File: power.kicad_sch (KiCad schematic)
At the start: 53 parts, among them J10 Conn_01x02, J11 Solar_Cell, J2 USB_C_Receptacle_USB2.0_14P, J9 Battery_Cell, Q1 AO4882, Q3 AO4882, U2 BQ25798, U5 TPS6282x

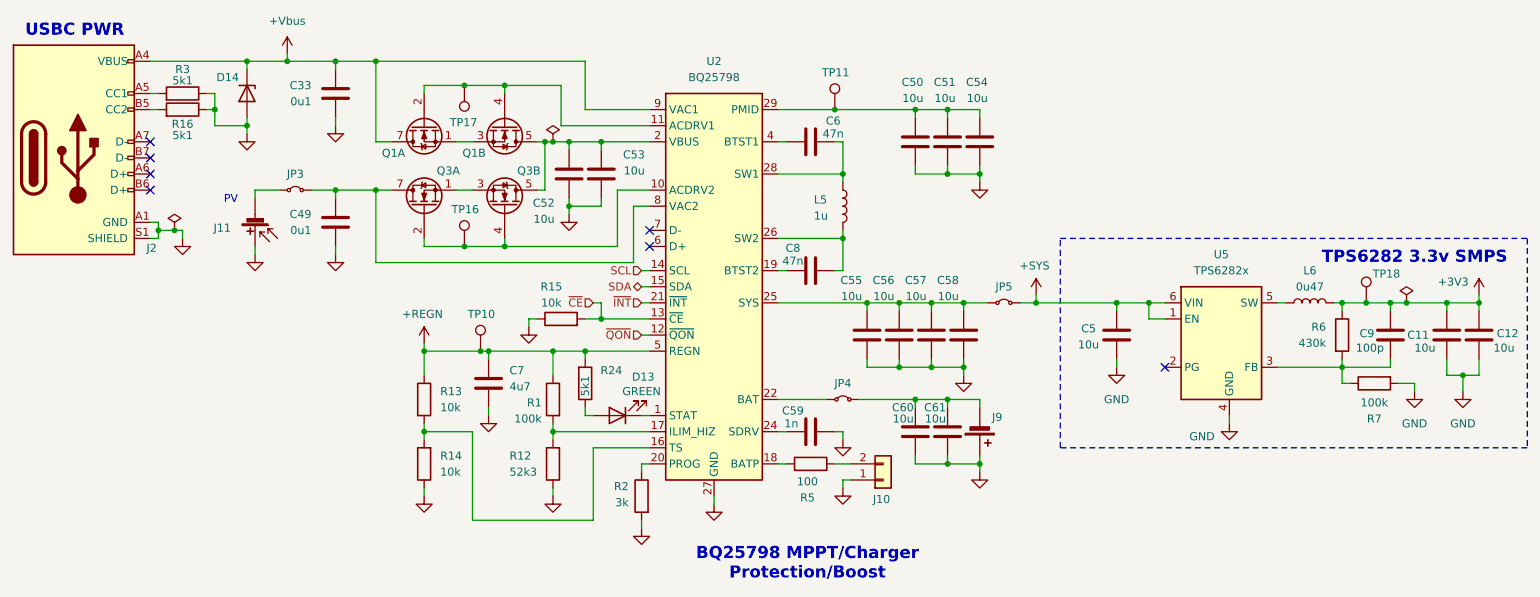
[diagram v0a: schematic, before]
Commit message: schem: renumber
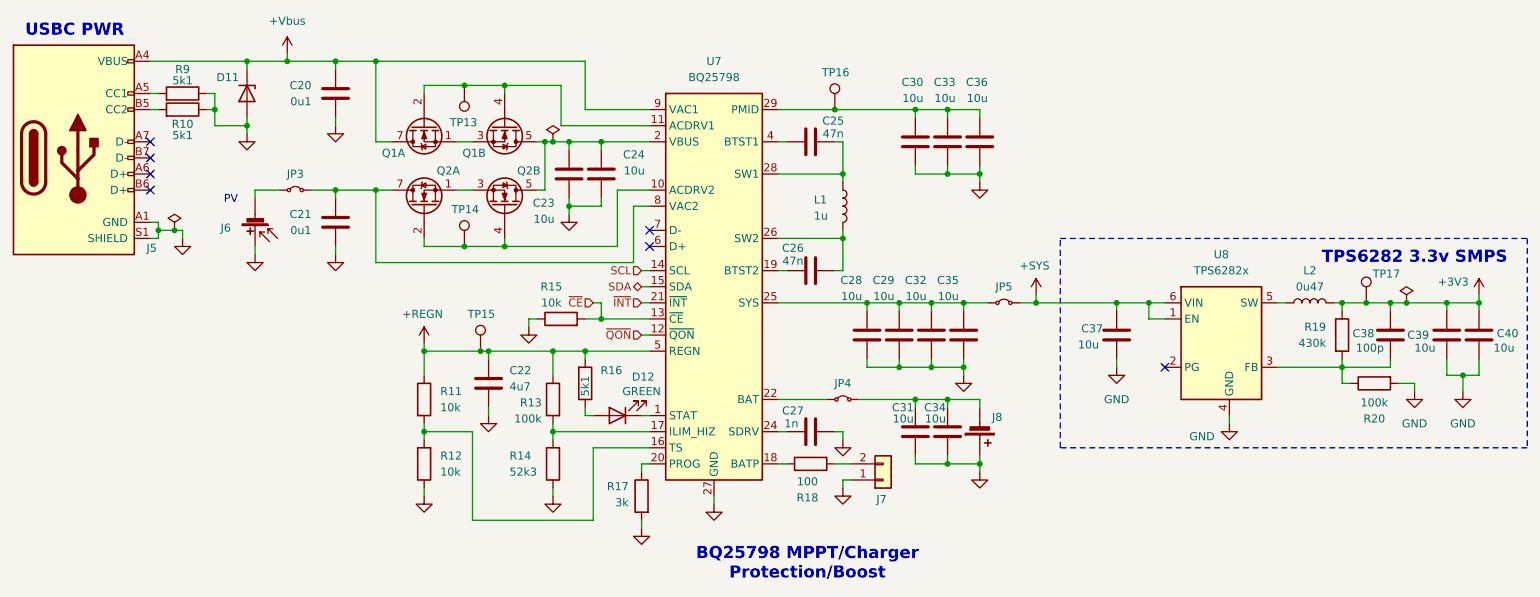
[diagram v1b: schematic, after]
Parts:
- renumbered C33 to C20, C49 to C21, C7 to C22, C52 to C23, C53 to C24, C6 to C25, C8 to C26, C59 to C27, C55 to C28, C56 to C29, C50 to C30, C60 to C31, C57 to C32, C51 to C33, C61 to C34, C58 to C35, C54 to C36, C5 to C37, C9 to C38, C11 to C39, C12 to C40, D14 to D11, D13 to D12, J2 to J5, J11 to J6, J10 to J7, J9 to J8, L5 to L1, L6 to L2, Q3 to Q2, R16 to R10, R13 to R11, R14 to R12, R1 to R13, R12 to R14, R24 to R16, R2 to R17, R5 to R18, R6 to R19, R7 to R20, R3 to R9, TP17 to TP13, TP16 to TP14, TP10 to TP15, TP11 to TP16, TP18 to TP17, U2 to U7, U5 to U8

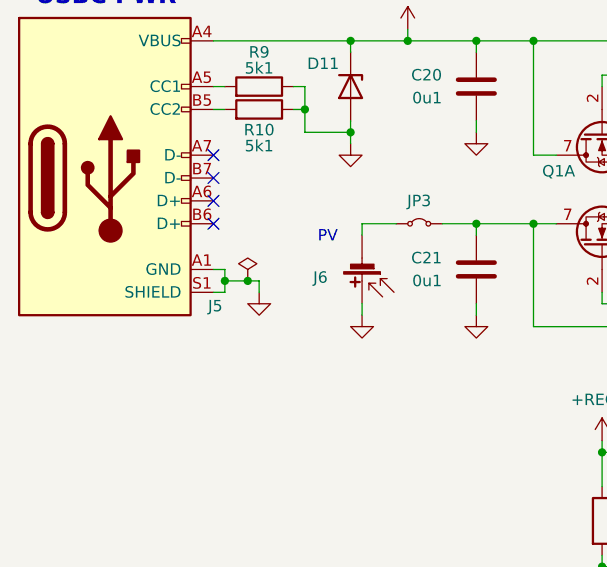
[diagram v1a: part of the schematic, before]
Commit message: pcb: add missing 3d models
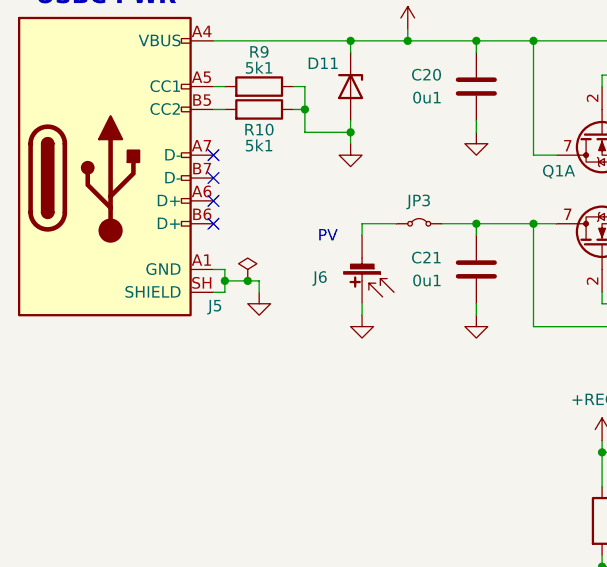
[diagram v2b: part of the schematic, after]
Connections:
- net GND: now also J5.SH (SHIELD); no longer J5.S1 (SHIELD)
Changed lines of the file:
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@@
 		(pin "A1"
 		)
-		(pin "S1"
+		(pin "SH"
 		)
 		(pin "B9"

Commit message: schem: add title to other sheet
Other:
- company: (none) -> Rémi Ait-Younes
- title: (none) -> Carte Meteo Lora 1
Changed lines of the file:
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@@
 	(generator_version "10.0")
 	(paper "A4")
+	(title_block
+		(title "Carte Meteo Lora 1")
+		(date "2026-05-26")
+		(rev "01")
+		(company "Rémi Ait-Younes")
+	)
 	(rectangle
 		(start 203.2 92.71)

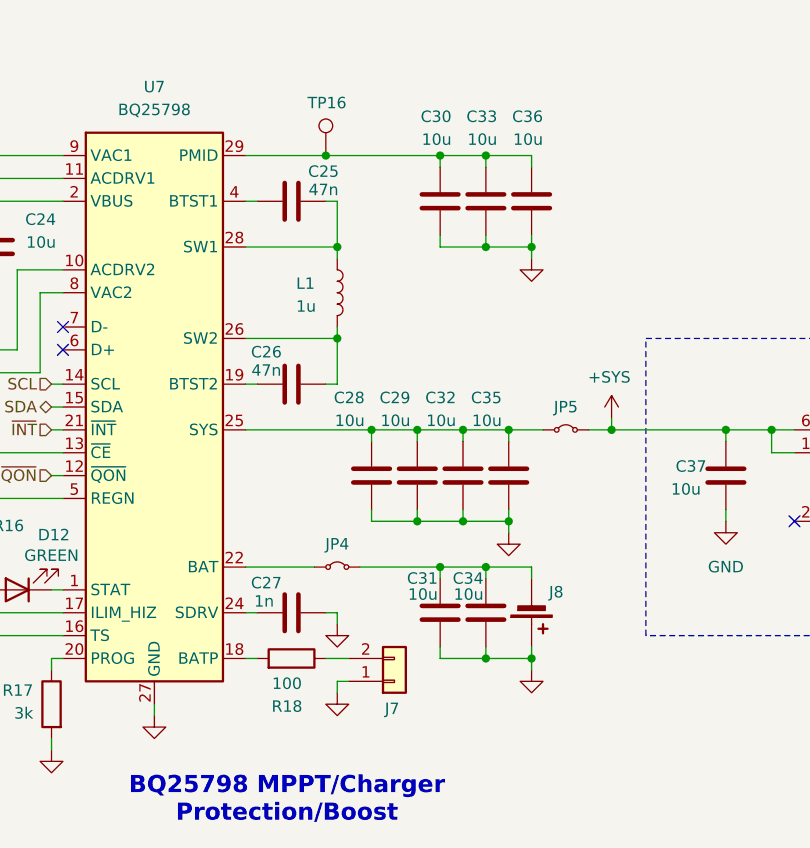
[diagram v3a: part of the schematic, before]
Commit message: pcb: add solar charger layout
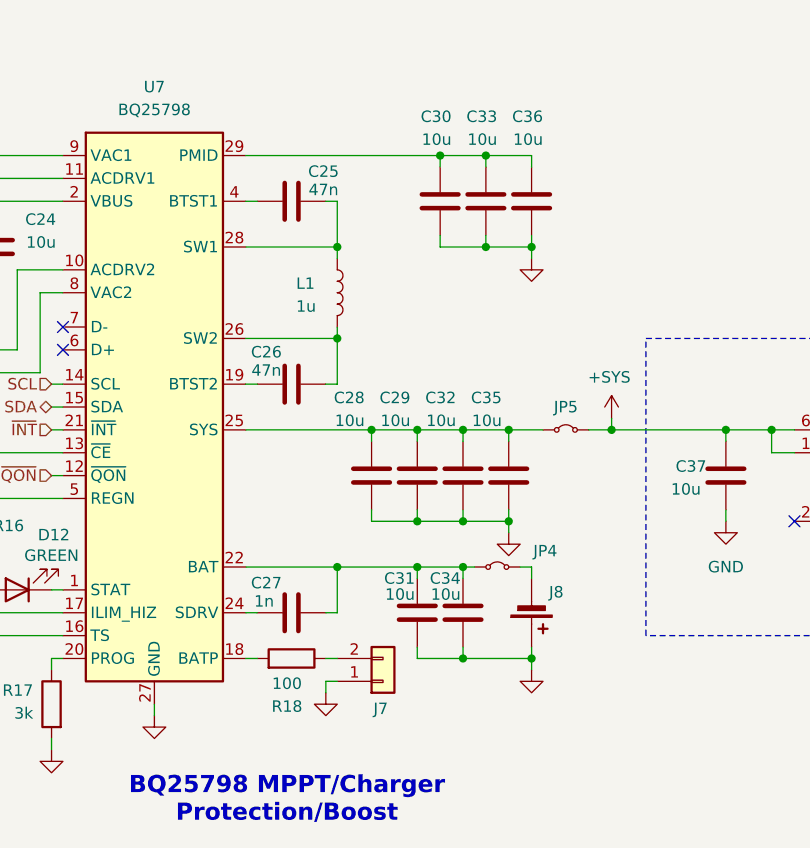
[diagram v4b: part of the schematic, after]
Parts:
- removed TP16: TestPoint, TestPoint:TestPoint_Pad_D2.0mm, symbol Connector:TestPoint
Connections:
- net GND: no longer C27.2
- net at JP4.1 (A), U7.22 (BAT), U7.23 (BAT): now also C27.2, C31.1, C34.1
- net at J8.2 (-), JP4.2 (B): no longer C31.1, C34.1
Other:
- moved on the sheet: C31, C34, J7
